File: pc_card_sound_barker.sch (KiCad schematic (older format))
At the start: 43 parts, among them IC1 MCP100-300D, IC2 74LVC1G00, IC3 MCP100-450D, IC4 TPA152DR, J1 IC1F-68RD-1.27SF(52), J2 Headphones Out, U1 Z8601720ASG, U2 25LCxxx, U3 YMF289B-S, U4 YAC516-E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

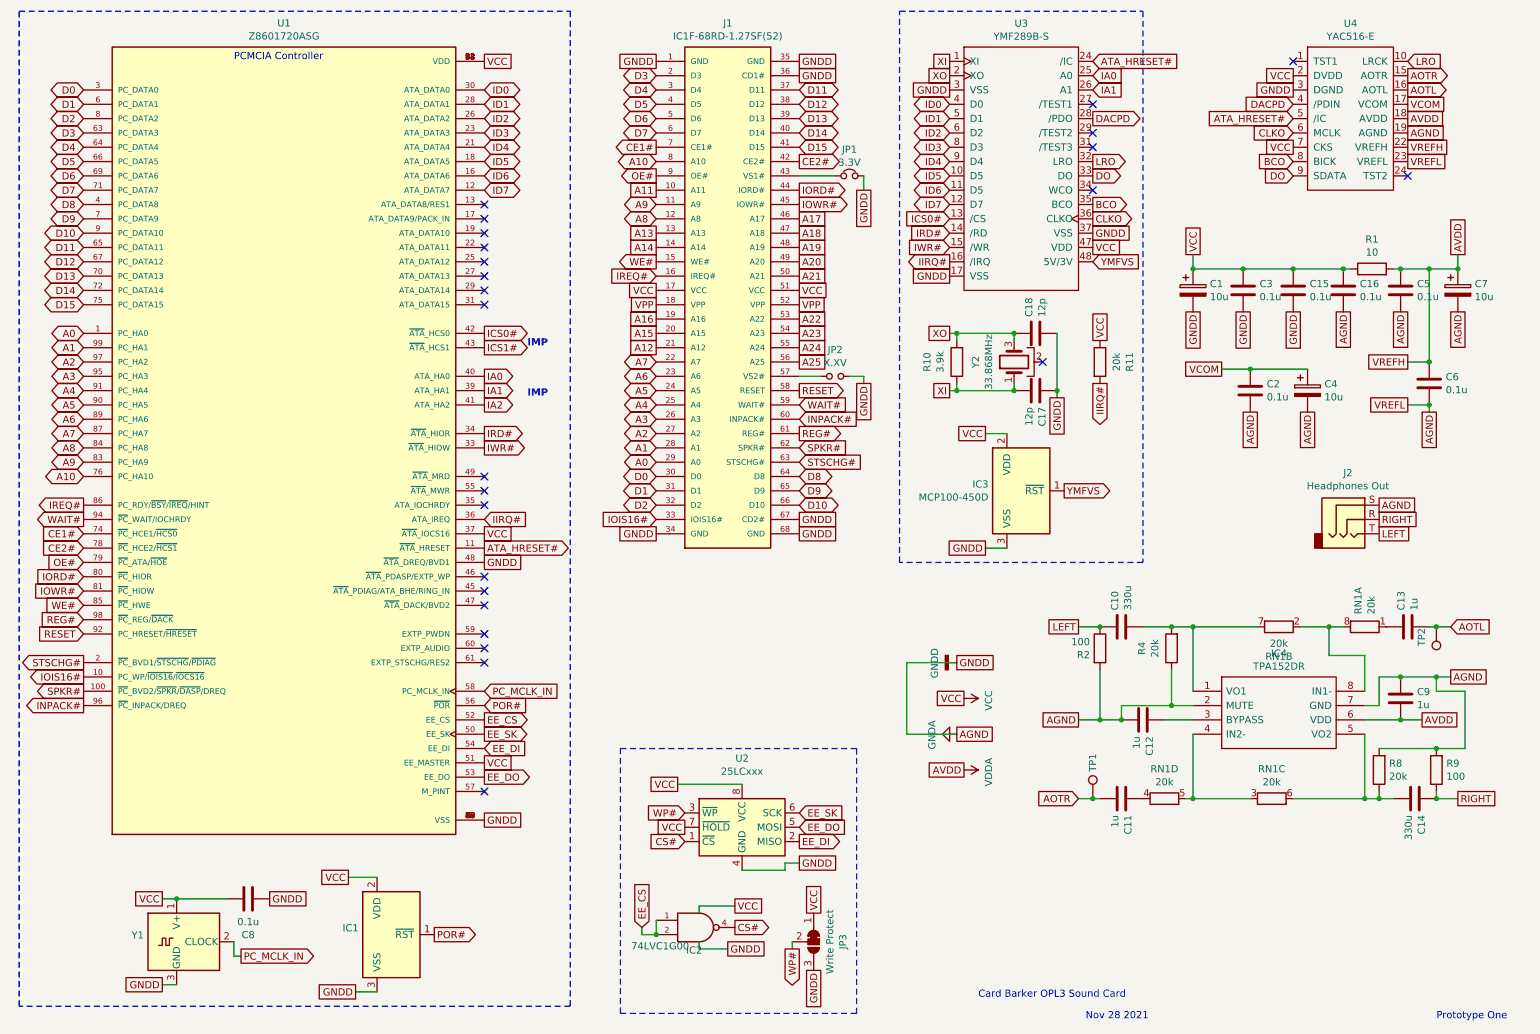
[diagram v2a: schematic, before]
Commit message: eeprom is isolated for onboard programming
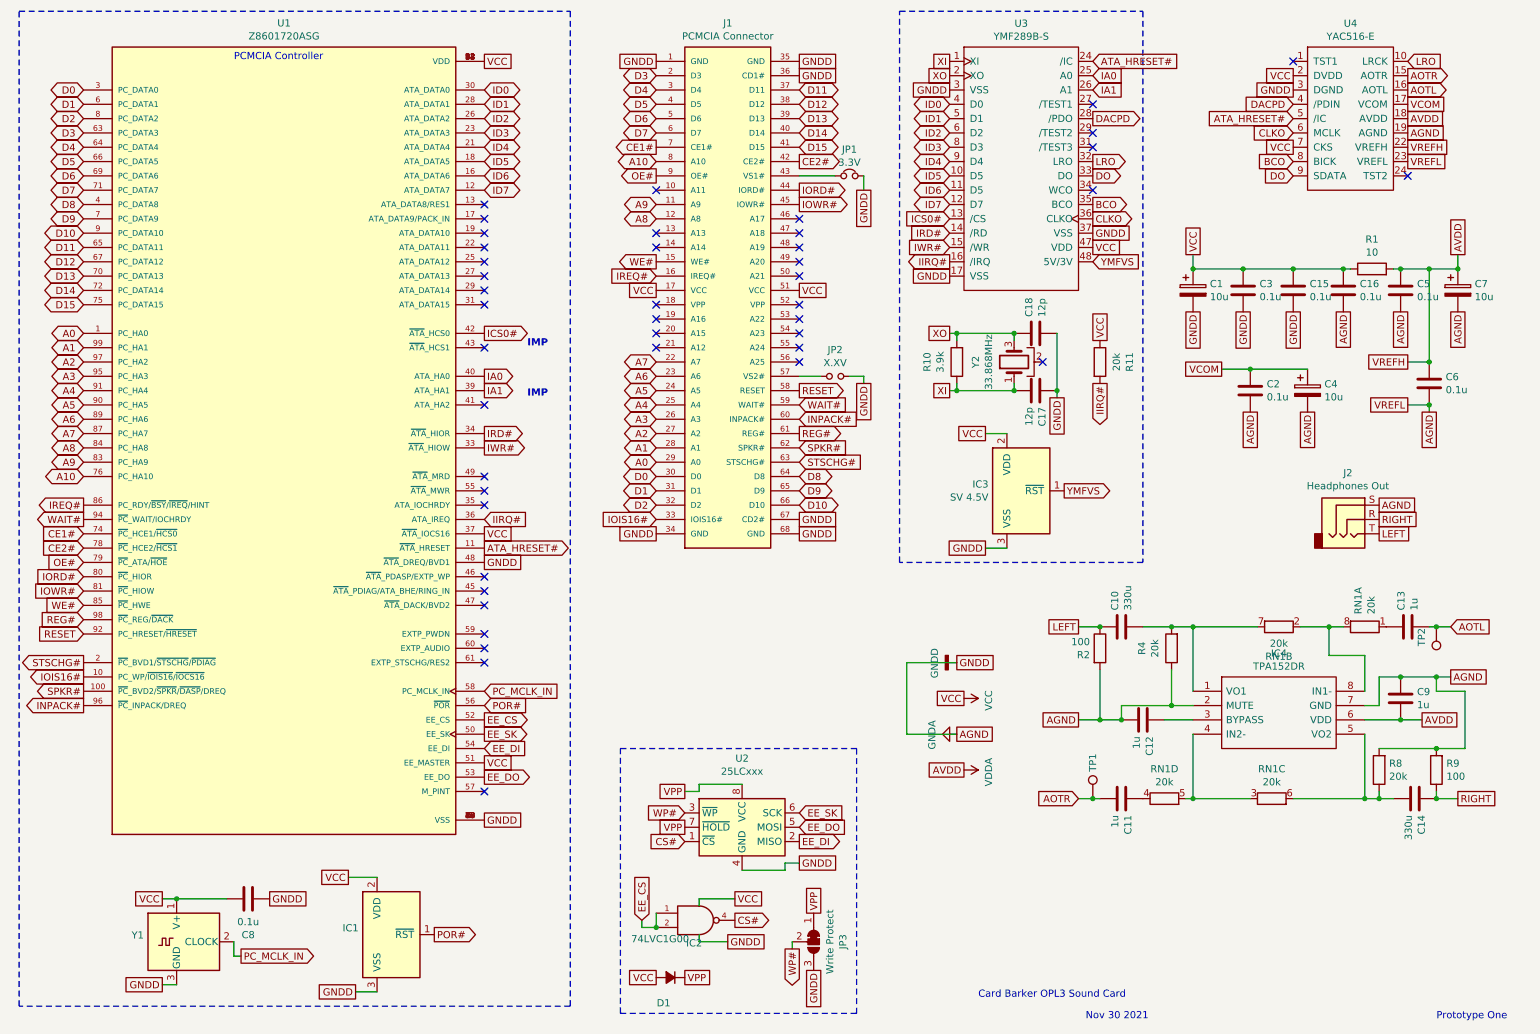
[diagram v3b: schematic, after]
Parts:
- added D1: D_Small_ALT, Diode_SMD:D_SOD-323_HandSoldering, symbol Device:D_Small_ALT
- IC1: value MCP100-300D -> SV 3.3V
- IC3: value MCP100-450D -> SV 4.5V
- J1: value IC1F-68RD-1.27SF(52) -> PCMCIA Connector
- U2: Manufacturer_Name (none) -> Microchip Technology
- Y1: value MAX7375AXR425 -> 4.19MHz; Manufacturer_Name (none) -> Maxim Integrated
- Y2: Manufacturer_Name (none) -> Murata Electronics
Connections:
- net VCC: now also D1.2 (A); no longer JP3.1 (A), U2.7 (~HOLD), U2.8 (VCC)
- net VPP: now also JP3.1 (A), U2.7 (~HOLD), U2.8 (VCC), D1.1 (K); no longer J1.18 (VPP), J1.52 (VPP)
- net A11: no longer names the net of J1.10 (A11)
- net A12: no longer names the net of J1.21 (A12)
- net A13: no longer names the net of J1.13 (A13)
- net A14: no longer names the net of J1.14 (A14)
- net A15: no longer names the net of J1.20 (A15)
- net A16: no longer names the net of J1.19 (A16)
- net A17: no longer names the net of J1.46 (A17)
- net A18: no longer names the net of J1.47 (A18)
- net A19: no longer names the net of J1.48 (A19)
- net A20: no longer names the net of J1.49 (A20)
- net A21: no longer names the net of J1.50 (A21)
- net A22: no longer names the net of J1.53 (A22)
- net A23: no longer names the net of J1.54 (A23)
- net A24: no longer names the net of J1.55 (A24)
- net A25: no longer names the net of J1.56 (A25)
- net IA2: no longer names the net of U1.41 (ATA_HA2)
- net ICS1#: no longer names the net of U1.43 (~ATA~_HCS1)
- no-connect marks 25 -> 44
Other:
- note added: "Nov 30 2021"
- note removed: "Nov 28 2021"
- moved on the sheet: IC2
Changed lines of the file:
@@
 P 5600 2550
 F 0 "J1" H 5600 4417 50  0000 C CNN
-F 1 "IC1F-68RD-1.27SF(52)" H 5600 4326 50  0000 C CNN
+F 1 "PCMCIA Connector" H 5600 4326 50  0000 C CNN
 F 2 "IC1F-68RD-1.27SF_52:IC1F-68RD-1.27SF(52)" H 5550 600 50  0001 L BNN
 F 3 "https://www.mouser.co.uk/datasheet/2/185/hirose_electric_hiros11303-1-1735566.pdf" H 5550 600 50  0001 L BNN
@@
 Text GLabel 3900 6250 2    50   UnSpc ~ 0
 GNDD
-Text GLabel 6100 6200 2    50   Input ~ 0
-EE_SK
 Text GLabel 3900 5650 2    50   Output ~ 0
 EE_SK
 Text GLabel 3900 5950 2    50   Output ~ 0
-EE_DO
-Text GLabel 6100 6400 2    50   Output ~ 0
-EE_DI
-Text GLabel 6100 6300 2    50   Input ~ 0
 EE_DO
 Text GLabel 3900 5750 2    50   Input ~ 0
@@
 GNDD
 Text GLabel 6200 6900 1    50   UnSpc ~ 0
-VCC
+VPP
 Text GLabel 3900 5850 2    50   UnSpc ~ 0
 VCC
@@
 Text GLabel 3900 3250 2    50   Output ~ 0
 IA1
-Text GLabel 3900 3350 2    50   Output ~ 0
-IA2
 Text GLabel 7150 2050 0    50   Input ~ 0
 ICS0#
@@
 Text GLabel 10350 1050 2    50   Output ~ 0
 AOTR
-Text GLabel 3900 2950 2    50   Output ~ 0
-ICS1#
 $Comp
 L YMF_YAC:YMF289B-S U3
@@
 Text GLabel 10350 1250 2    50   UnSpc ~ 0
 VCOM
-Wire Wire Line
-	5700 6000 5250 6000
-Text GLabel 5250 6000 0    50   UnSpc ~ 0
-VCC
-Text GLabel 5300 6300 0    50   UnSpc ~ 0
-VCC
-Text GLabel 5300 6200 0    50   Input ~ 0
-WP#
 Text GLabel 10350 1650 2    50   UnSpc ~ 0
 VREFL
@@
 Text GLabel 9200 2700 3    50   UnSpc ~ 0
 GNDD
-Text GLabel 6100 2650 2    50   UnSpc ~ 0
-VPP
-Text GLabel 5100 2650 0    50   UnSpc ~ 0
-VPP
 Wire Wire Line
 	6250 3150 6100 3150
@@
 F 5 "81-XRCPB33M868F0L0R0" H 7600 3050 50  0001 C CNN "Mouser Part Number"
 F 6 "https://www.mouser.co.uk/ProductDetail/81-XRCPB33M868F0L0R0" H 7600 3050 50  0001 C CNN "Mouser Price/Stock"
+F 7 "Murata Electronics" H 7600 3050 50  0001 C CNN "Manufacturer_Name"
 	1    7600 3050
 	0    -1   -1   0
@@
 P 3250 7050
 F 0 "IC1" H 3021 7096 50  0000 R CNN
-F 1 "MCP100-300D" H 3021 7005 50  0001 R CNN
+F 1 "SV 3.3V" H 3021 7005 50  0001 R CNN
 F 2 "Package_TO_SOT_SMD:SOT-23" H 2850 7200 50  0001 C CNN
 F 3 "https://www.ti.com/lit/ds/symlink/tlv803e.pdf" H 2950 7300 50  0001 C CNN
@@
 Wire Notes Line
 	6800 4450 6800 600
-Wire Notes Line
-	4850 5750 6500 5750
 Wire Notes Line
 	6500 5750 6500 7600
@@
 P 1750 7100
 F 0 "Y1" H 1521 7146 50  0000 R CNN
-F 1 "MAX7375AXR425" H 1521 7055 50  0001 R CNN
+F 1 "4.19MHz" H 1521 7055 50  0001 R CNN
 F 2 "Package_TO_SOT_SMD:SOT-323_SC-70" H 2850 6750 50  0001 C CNN
 F 3 "https://datasheets.maximintegrated.com/en/ds/MAX7375.pdf" H 1650 7100 50  0001 C CNN
@@
 F 5 "700-MAX7375AXR425T" H 1750 7100 50  0001 C CNN "Mouser Part Number"
 F 6 "https://www.mouser.co.uk/ProductDetail/700-MAX7375AXR425T" H 1750 7100 50  0001 C CNN "Mouser Price/Stock"
+F 7 "Maxim Integrated" H 1750 7100 50  0001 C CNN "Manufacturer_Name"
 	1    1750 7100
 	1    0    0    -1
@@
 Wire Wire Line
 	6050 7150 6050 7100
-Text GLabel 5300 6400 0    50   Input ~ 0
-CS#
 Text GLabel 3900 5550 2    50   Output ~ 0
 EE_CS
@@
 P 7650 3950
 F 0 "IC3" H 7421 3996 50  0000 R CNN
-F 1 "MCP100-450D" H 7421 3905 50  0000 R CNN
+F 1 "SV 4.5V" H 7421 3905 50  0000 R CNN
 F 2 "Package_TO_SOT_SMD:SOT-23" H 7250 4100 50  0001 C CNN
 F 3 "https://www.ti.com/lit/ds/symlink/tlv809e.pdf" H 7350 4200 50  0001 C CNN
@@
 	1    0    0    -1
 $EndComp
-$Comp
-L Memory_EEPROM:25LCxxx U2
-U 1 1 619EBE92
-P 5700 6300
-F 0 "U2" H 5700 6781 50  0000 C CNN
-F 1 "25LCxxx" H 5700 6690 50  0000 C CNN
-F 2 "Package_SO:SOIC-8_3.9x4.9mm_P1.27mm" H 5700 6300 50  0001 C CNN
-F 3 "http://ww1.microchip.com/downloads/en/DeviceDoc/21832H.pdf" H 5700 6300 50  0001 C CNN
-F 4 "25LC020A-E/SN" H 5700 6300 50  0001 C CNN "Manufacturer_Part_Number"
-F 5 "579-25LC020A-E/SN" H 5700 6300 50  0001 C CNN "Mouser Part Number"
-F 6 "https://www.mouser.co.uk/ProductDetail/579-25LC020A-E-SN" H 5700 6300 50  0001 C CNN "Mouser Price/Stock"
-	1    5700 6300
-	1    0    0    -1
-$EndComp
-$Comp
-L 74xGxx:74LVC1G00 IC2
-U 1 1 61B9D486
-P 5400 7000
-F 0 "IC2" H 5421 6870 50  0000 R TNN
-F 1 "74LVC1G00" H 5330 6870 50  0000 R CNN
-F 2 "Package_TO_SOT_SMD:SOT-23-5_HandSoldering" H 5400 7000 50  0001 C CNN
-F 3 "https://www.ti.com/lit/ds/symlink/sn74lvc1g38.pdf" H 5400 7000 50  0001 C CNN
-F 4 "Texas Instruments" H 5400 7000 50  0001 C CNN "Manufacturer_Name"
-F 5 "SN74LVC1G38DBVRE4" H 5400 7000 50  0001 C CNN "Manufacturer_Part_Number"
-F 6 "595-74LVC1G38DBVRE4" H 5400 7000 50  0001 C CNN "Mouser Part Number"
-	1    5400 7000
-	1    0    0    -1
-$EndComp
-Text GLabel 5600 7150 2    50   UnSpc ~ 0
-GNDD
-Text GLabel 5650 6850 2    50   UnSpc ~ 0
-VCC
-Text GLabel 5650 7000 2    50   Output ~ 0
-CS#
-Text GLabel 5000 7000 1    50   Input ~ 0
-EE_CS
-Wire Wire Line
-	5100 6950 5100 7050
-Wire Wire Line
-	5100 7050 5000 7050
-Wire Wire Line
-	5000 7050 5000 7000
-Connection ~ 5100 7050
-Wire Wire Line
-	5600 7150 5400 7150
-Wire Wire Line
-	5400 7150 5400 7100
-Wire Wire Line
-	5650 6850 5400 6850
-Wire Wire Line
-	5400 6850 5400 6900
 NoConn ~ 3900 3850
 NoConn ~ 3900 3950
@@
 NoConn ~ 3900 2050
 NoConn ~ 3900 1950
-Text GLabel 6100 2050 2    50   UnSpc ~ 0
-A17
-Text GLabel 5100 1850 0    50   UnSpc ~ 0
-A11
-Text GLabel 5100 2150 0    50   UnSpc ~ 0
-A13
-Text GLabel 6100 2150 2    50   UnSpc ~ 0
-A18
-Text GLabel 5100 2250 0    50   UnSpc ~ 0
-A14
-Text GLabel 6100 2350 2    50   UnSpc ~ 0
-A20
-Text GLabel 6100 2450 2    50   UnSpc ~ 0
-A21
-Text GLabel 6100 2250 2    50   UnSpc ~ 0
-A19
-Text GLabel 5100 2750 0    50   UnSpc ~ 0
-A16
-Text GLabel 6100 2750 2    50   UnSpc ~ 0
-A22
-Text GLabel 5100 2850 0    50   UnSpc ~ 0
-A15
-Text GLabel 5100 2950 0    50   UnSpc ~ 0
-A12
-Text GLabel 6100 2850 2    50   UnSpc ~ 0
-A23
-Text GLabel 6100 2950 2    50   UnSpc ~ 0
-A24
-Text GLabel 6100 3050 2    50   UnSpc ~ 0
-A25
 Wire Notes Line
 	4500 600  4500 7550
@@
 	650  600  4500 600
 NoConn ~ 8150 1850
-Text GLabel 6100 6550 2    50   UnSpc ~ 0
-GNDD
-Wire Wire Line
-	5700 6600 6000 6600
-Wire Wire Line
-	6000 6600 6000 6550
-Wire Wire Line
-	6000 6550 6100 6550
 NoConn ~ 7800 3050
 NoConn ~ 3900 4550
@@
 Card Barker OPL3 Sound Card
 Text Notes 8100 7650 0    50   ~ 0
-Nov 28 2021
+Nov 30 2021
 Text Notes 10550 7650 0    50   ~ 0
 Prototype One
@@
 	1    0    0    -1
 $EndComp
+NoConn ~ 6100 3050
+NoConn ~ 6100 2950
+NoConn ~ 6100 2850
+NoConn ~ 6100 2750
+NoConn ~ 6100 2450
+NoConn ~ 6100 2350
+NoConn ~ 6100 2250
+NoConn ~ 6100 2150
+NoConn ~ 6100 2050
+NoConn ~ 5100 2150
+NoConn ~ 5100 2250
+NoConn ~ 5100 2750
+NoConn ~ 5100 2850
+NoConn ~ 5100 2950
+NoConn ~ 5100 1850
+NoConn ~ 3900 3350
+NoConn ~ 3900 2950
+Wire Wire Line
+	5400 6800 5400 6850
+Wire Wire Line
+	5650 6800 5400 6800
+Wire Wire Line
+	5400 7100 5400 7050
+Wire Wire Line
+	5600 7100 5400 7100
+Connection ~ 5100 7000
+Wire Wire Line
+	5000 7000 5000 6950
+Wire Wire Line
+	5100 7000 5000 7000
+Wire Wire Line
+	5100 6900 5100 7000
+Text GLabel 5000 6950 1    50   Input ~ 0
+EE_CS
+Text GLabel 5650 6950 2    50   Output ~ 0
+CS#
+Text GLabel 5650 6800 2    50   UnSpc ~ 0
+VCC
+Text GLabel 5600 7100 2    50   UnSpc ~ 0
+GNDD
+$Comp
+L 74xGxx:74LVC1G00 IC2
+U 1 1 61B9D486
+P 5400 6950
+F 0 "IC2" H 5421 6820 50  0000 R TNN
+F 1 "74LVC1G00" H 5330 6820 50  0000 R CNN
+F 2 "Package_TO_SOT_SMD:SOT-23-5_HandSoldering" H 5400 6950 50  0001 C CNN
+F 3 "https://www.ti.com/lit/ds/symlink/sn74lvc1g38.pdf" H 5400 6950 50  0001 C CNN
+F 4 "Texas Instruments" H 5400 6950 50  0001 C CNN "Manufacturer_Name"
+F 5 "SN74LVC1G38DBVRE4" H 5400 6950 50  0001 C CNN "Manufacturer_Part_Number"
+F 6 "595-74LVC1G38DBVRE4" H 5400 6950 50  0001 C CNN "Mouser Part Number"
+	1    5400 6950
+	1    0    0    -1
+$EndComp
+Wire Wire Line
+	5400 6000 5700 6000
+$Comp
+L Device:D_Small_ALT D1
+U 1 1 61ACC60B
+P 5200 7350
+F 0 "D1" H 5200 7557 50  0000 L TNN
+F 1 "D_Small_ALT" H 5200 7466 50  0001 C CNN
+F 2 "Diode_SMD:D_SOD-323_HandSoldering" V 5200 7350 50  0001 C CNN
+F 3 "https://www.mouser.co.uk/datasheet/2/258/BAV19WS_BAV21WS_SOD_323_-2510325.pdf" V 5200 7350 50  0001 C CNN
+F 4 "MCC" H 5200 7350 50  0001 C CNN "Manufacturer_Name"
+F 5 "BAV19WS-TP" H 5200 7350 50  0001 C CNN "Manufacturer_Part_Number"
+F 6 "833-BAV19WS-TP" H 5200 7350 50  0001 C CNN "Mouser Part Number"
+	1    5200 7350
+	-1   0    0    1
+$EndComp
+Text GLabel 6100 6200 2    50   Input ~ 0
+EE_SK
+Text GLabel 6100 6400 2    50   Output ~ 0
+EE_DI
+Text GLabel 6100 6300 2    50   Input ~ 0
+EE_DO
+Text GLabel 5100 7350 0    50   UnSpc ~ 0
+VCC
+Text GLabel 5300 6300 0    50   UnSpc ~ 0
+VPP
+Text GLabel 5300 6200 0    50   Input ~ 0
+WP#
+Text GLabel 5300 6400 0    50   Input ~ 0
+CS#
+$Comp
+L Memory_EEPROM:25LCxxx U2
+U 1 1 619EBE92
+P 5700 6300
+F 0 "U2" H 5700 6781 50  0000 C CNN
+F 1 "25LCxxx" H 5700 6690 50  0000 C CNN
+F 2 "Package_SO:SOIC-8_3.9x4.9mm_P1.27mm" H 5700 6300 50  0001 C CNN
+F 3 "http://ww1.microchip.com/downloads/en/DeviceDoc/21832H.pdf" H 5700 6300 50  0001 C CNN
+F 4 "25LC020A-E/SN" H 5700 6300 50  0001 C CNN "Manufacturer_Part_Number"
+F 5 "579-25LC020A-E/SN" H 5700 6300 50  0001 C CNN "Mouser Part Number"
+F 6 "https://www.mouser.co.uk/ProductDetail/579-25LC020A-E-SN" H 5700 6300 50  0001 C CNN "Mouser Price/Stock"
+F 7 "Microchip Technology " H 5700 6300 50  0001 C CNN "Manufacturer_Name"
+	1    5700 6300
+	1    0    0    -1
+$EndComp
+Text GLabel 6100 6550 2    50   UnSpc ~ 0
+GNDD
+Wire Wire Line
+	5700 6600 6000 6600
+Wire Wire Line
+	6000 6600 6000 6550
+Wire Wire Line
+	6000 6550 6100 6550
+Wire Notes Line
+	4850 5750 6500 5750
+Text GLabel 5300 7350 2    50   UnSpc ~ 0
+VPP
+Text GLabel 5300 6050 0    50   UnSpc ~ 0
+VPP
+Wire Wire Line
+	5300 6050 5400 6050
+Wire Wire Line
+	5400 6050 5400 6000
+NoConn ~ 6100 2650
+NoConn ~ 5100 2650
 $EndSCHEMATC
